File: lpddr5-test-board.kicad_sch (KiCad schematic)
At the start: 13 parts, among them M1 1296.2013

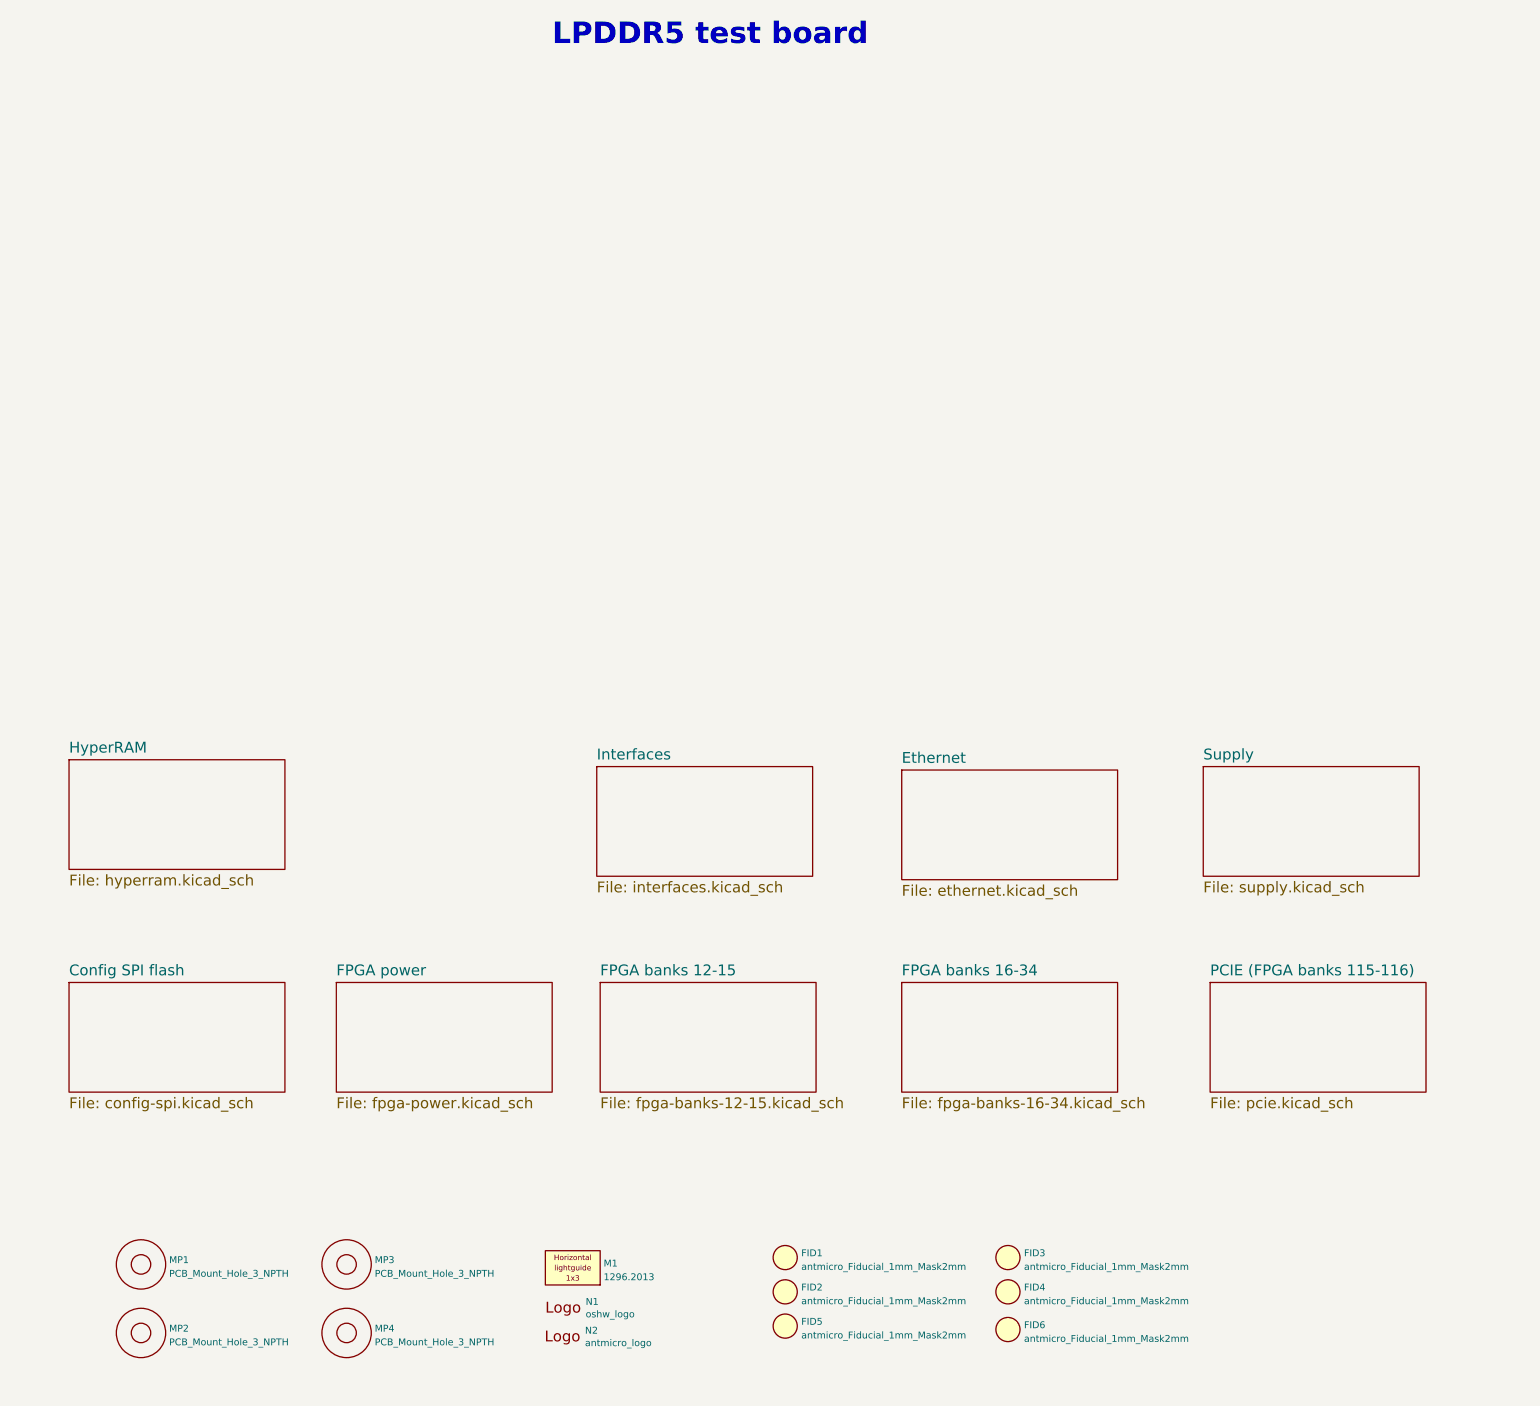
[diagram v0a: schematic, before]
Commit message: Rebase to Rev. 1.2.2
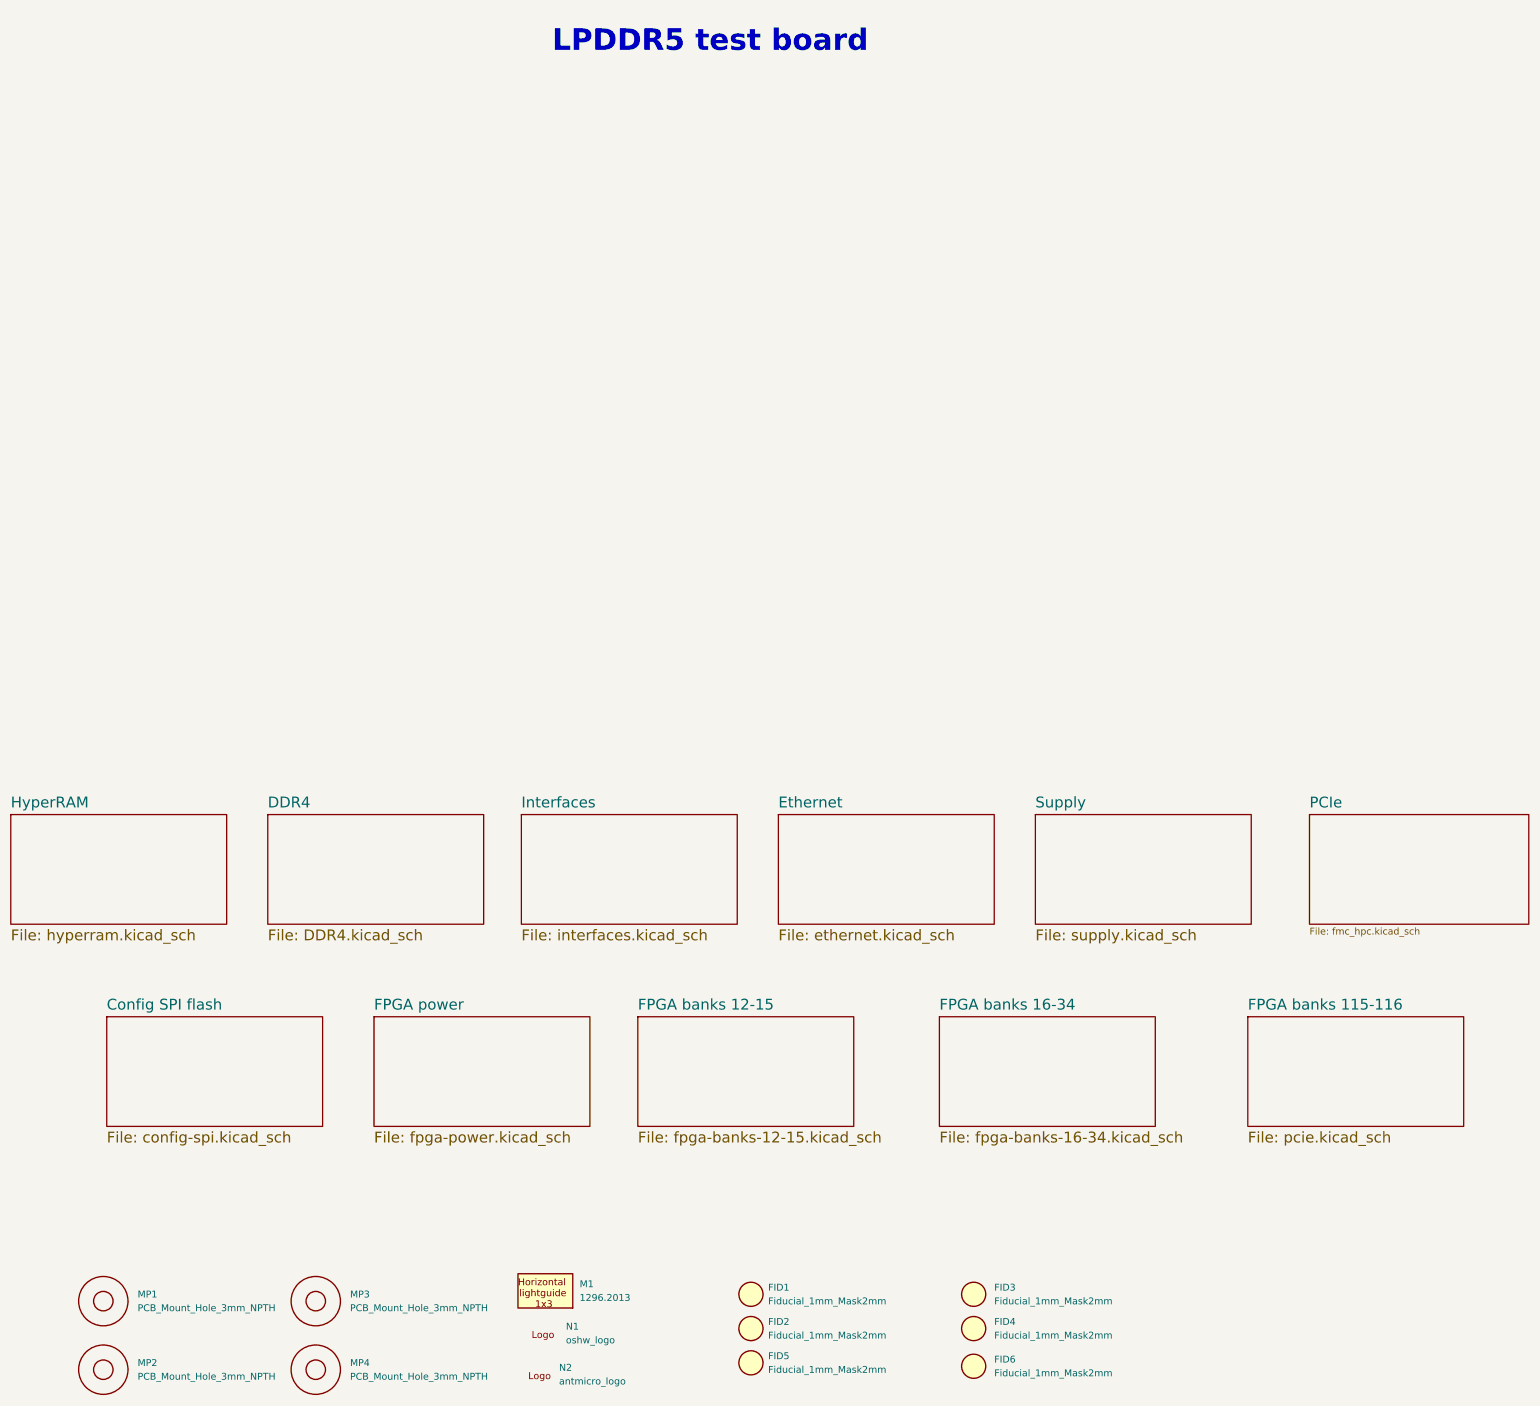
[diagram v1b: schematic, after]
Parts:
- removed FID1, FID2, FID3, FID4, FID5, FID6: antmicro_Fiducial_1mm_Mask2mm, antmicro-footprints:Fiducial_1mm_Mask2mm, symbol antmicroFiducialMarks:antmicro_Fiducial_1mm_Mask2mm
- removed M1: 1296.2013, antmicro-footprints:Mentor_1296.2013, symbol antmicroMechanicalParts:1296.2013
- removed MP1, MP2, MP3, MP4: PCB_Mount_Hole_3_NPTH, antmicro-footprints:mounting-hole-3mm-NPTH, symbol antmicroMechanicalParts:PCB_Mount_Hole_3_NPTH
- removed N1: oshw_logo, antmicro-footprints:OSHW-Logo_5.7x6mm_Mask, symbol data-center-dram-tester:oshw_logo
- removed N2: antmicro_logo, antmicro-footprints:antmicro-logo_scaled_20mm_mask, symbol data-center-dram-tester:antmicro_logo
- added FID1, FID2, FID3, FID4, FID5, FID6: Fiducial_1mm_Mask2mm, data-center-rdimm-ddr4-tester-footprints:Fiducial_1mm_Mask2mm, symbol data-center-rdimm-ddr4-tester:Fiducial_1mm_Mask2mm
- added M1: Mech_Lightpipe_Mentor_1296.2013, data-center-rdimm-ddr4-tester-footprints:Mech_Lightpipe_Mentor_1296.2013, symbol data-center-rdimm-ddr4-tester:Mech_Lightpipe_Mentor_1296.2013
- added MP1, MP2, MP3, MP4: PCB_Mount_Hole_3mm_NPTH, data-center-rdimm-ddr4-tester-footprints:mounting-hole-3mm-NPTH, symbol data-center-rdimm-ddr4-tester:PCB_Mount_Hole_3mm_NPTH
- added N1: oshw_logo, data-center-rdimm-ddr4-tester-footprints:oshw-logo, symbol data-center-rdimm-ddr4-tester:oshw_logo
- added N2: antmicro_logo, data-center-rdimm-ddr4-tester-footprints:antmicro-logo_scaled_20mm_mask, symbol data-center-rdimm-ddr4-tester:antmicro_logo
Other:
- removed sheet PCIE (FPGA banks 115-116)
- added sheet DDR4 (DDR4.kicad_sch)
- added sheet FPGA banks 115-116 (pcie.kicad_sch)
- added sheet PCIe (fmc_hpc.kicad_sch)

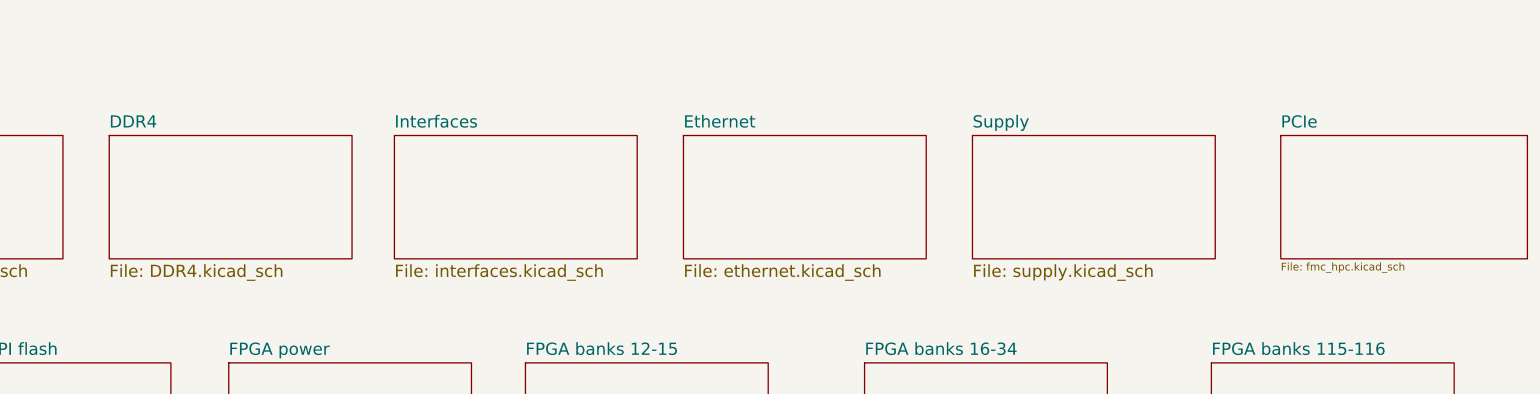
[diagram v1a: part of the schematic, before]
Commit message: Rename sheets for DDR5 and PCIe connectors
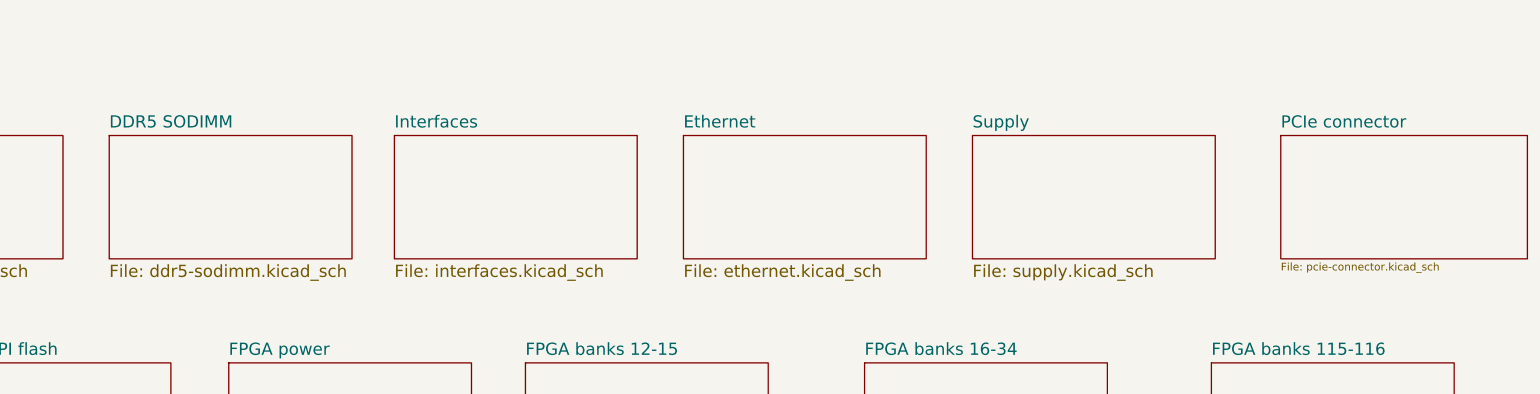
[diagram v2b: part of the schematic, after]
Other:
- sheet DDR4 renamed DDR5 SODIMM
- sheet PCIe renamed PCIe connector
- sheet DDR5 SODIMM: file DDR4.kicad_sch -> ddr5-sodimm.kicad_sch
- sheet PCIe connector: file fmc_hpc.kicad_sch -> pcie-connector.kicad_sch

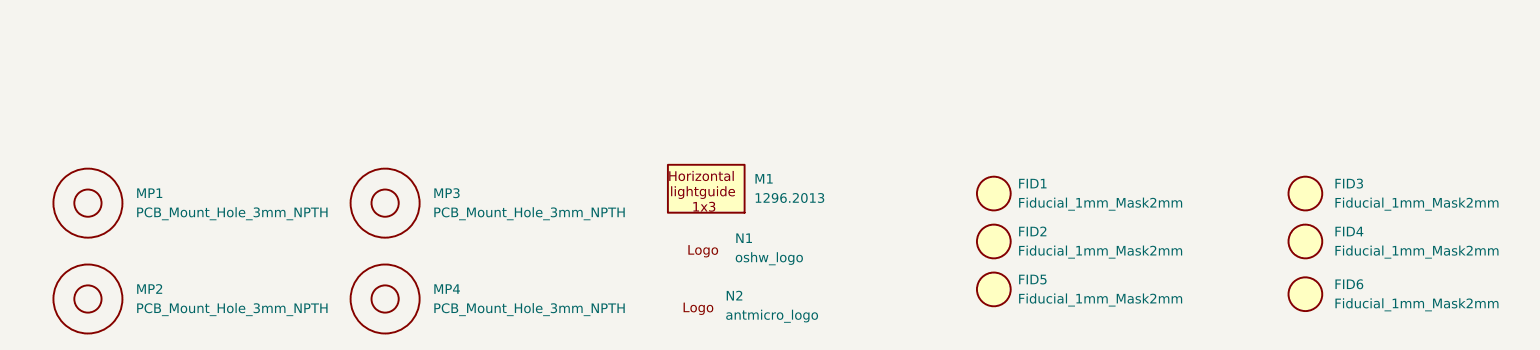
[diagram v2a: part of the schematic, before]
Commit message: Update designators and sync schematic with PCB
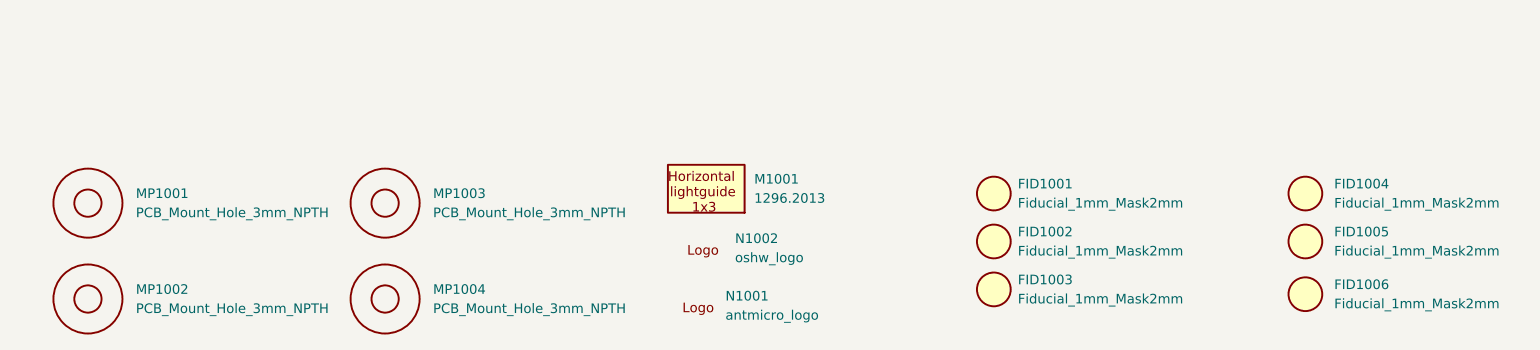
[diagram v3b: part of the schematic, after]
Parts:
- renumbered FID1 to FID1001, FID2 to FID1002, FID5 to FID1003, FID3 to FID1004, FID4 to FID1005, FID6 to FID1006, M1 to M1001, MP1 to MP1001, MP2 to MP1002, MP3 to MP1003, MP4 to MP1004, N2 to N1001, N1 to N1002
